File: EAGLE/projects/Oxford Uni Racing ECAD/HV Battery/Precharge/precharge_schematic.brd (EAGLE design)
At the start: 87.6 x 70.8 mm, 61 parts, among them IC1 TLV9001SIDCKR, IC10 74HC1G86GW-Q100H, IC11 74LVC1G32GV,125, IC2 TLV9001SIDCKR, IC3 TLV9001SIDCKR, IC4 TLV9001SIDCKR, IC5 LT1129CS8-3.3#PBF, IC6 LT1129CS8-3.3#PBF, IC7 LT1129CS8-3.3#PBF, IC8 LT1129CS8-3.3#PBF, IC9 74AHC1G08GV,125, J1 T816108A1S102CEU, Q1 BSS138, Q2 BSS138, U1 AMC1350QDWVRQ1AMC1350QDWVRQ1_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, U2 AMC1350QDWVRQ1AMC1350QDWVRQ1_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

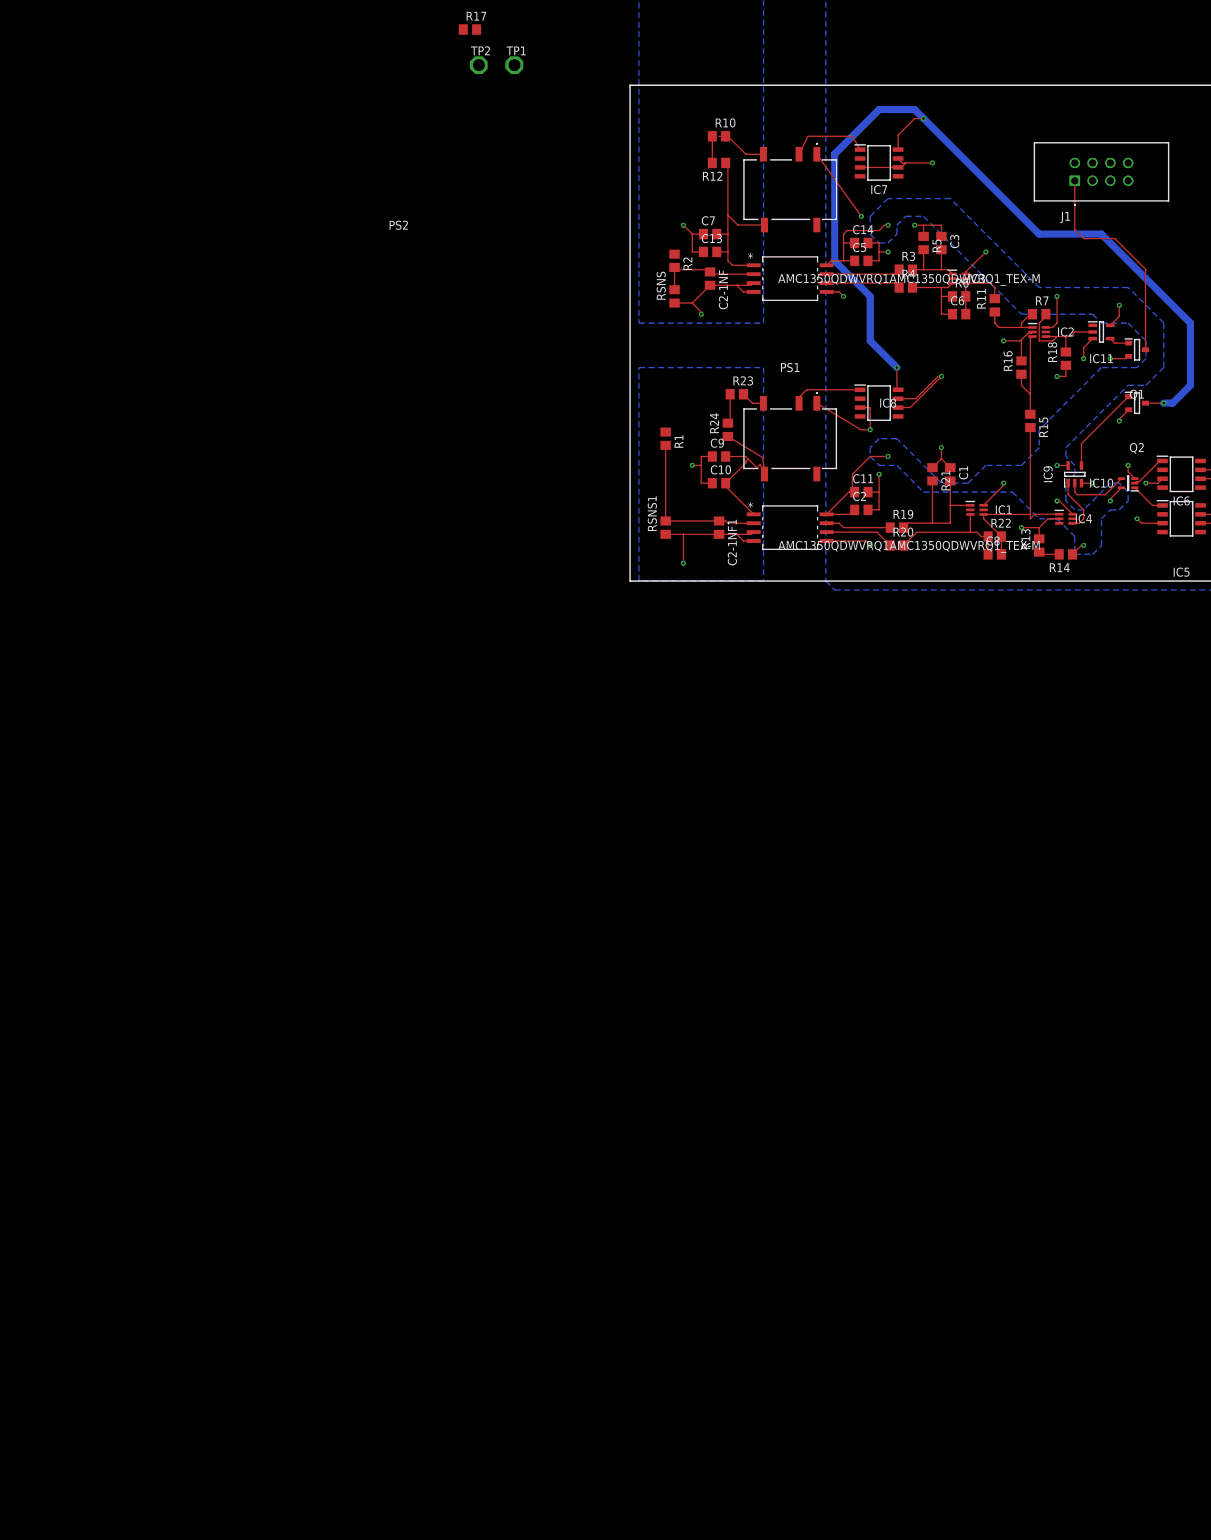
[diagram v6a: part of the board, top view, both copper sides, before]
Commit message: Library files + new main board/precharge board 8 pin mini-spox connector
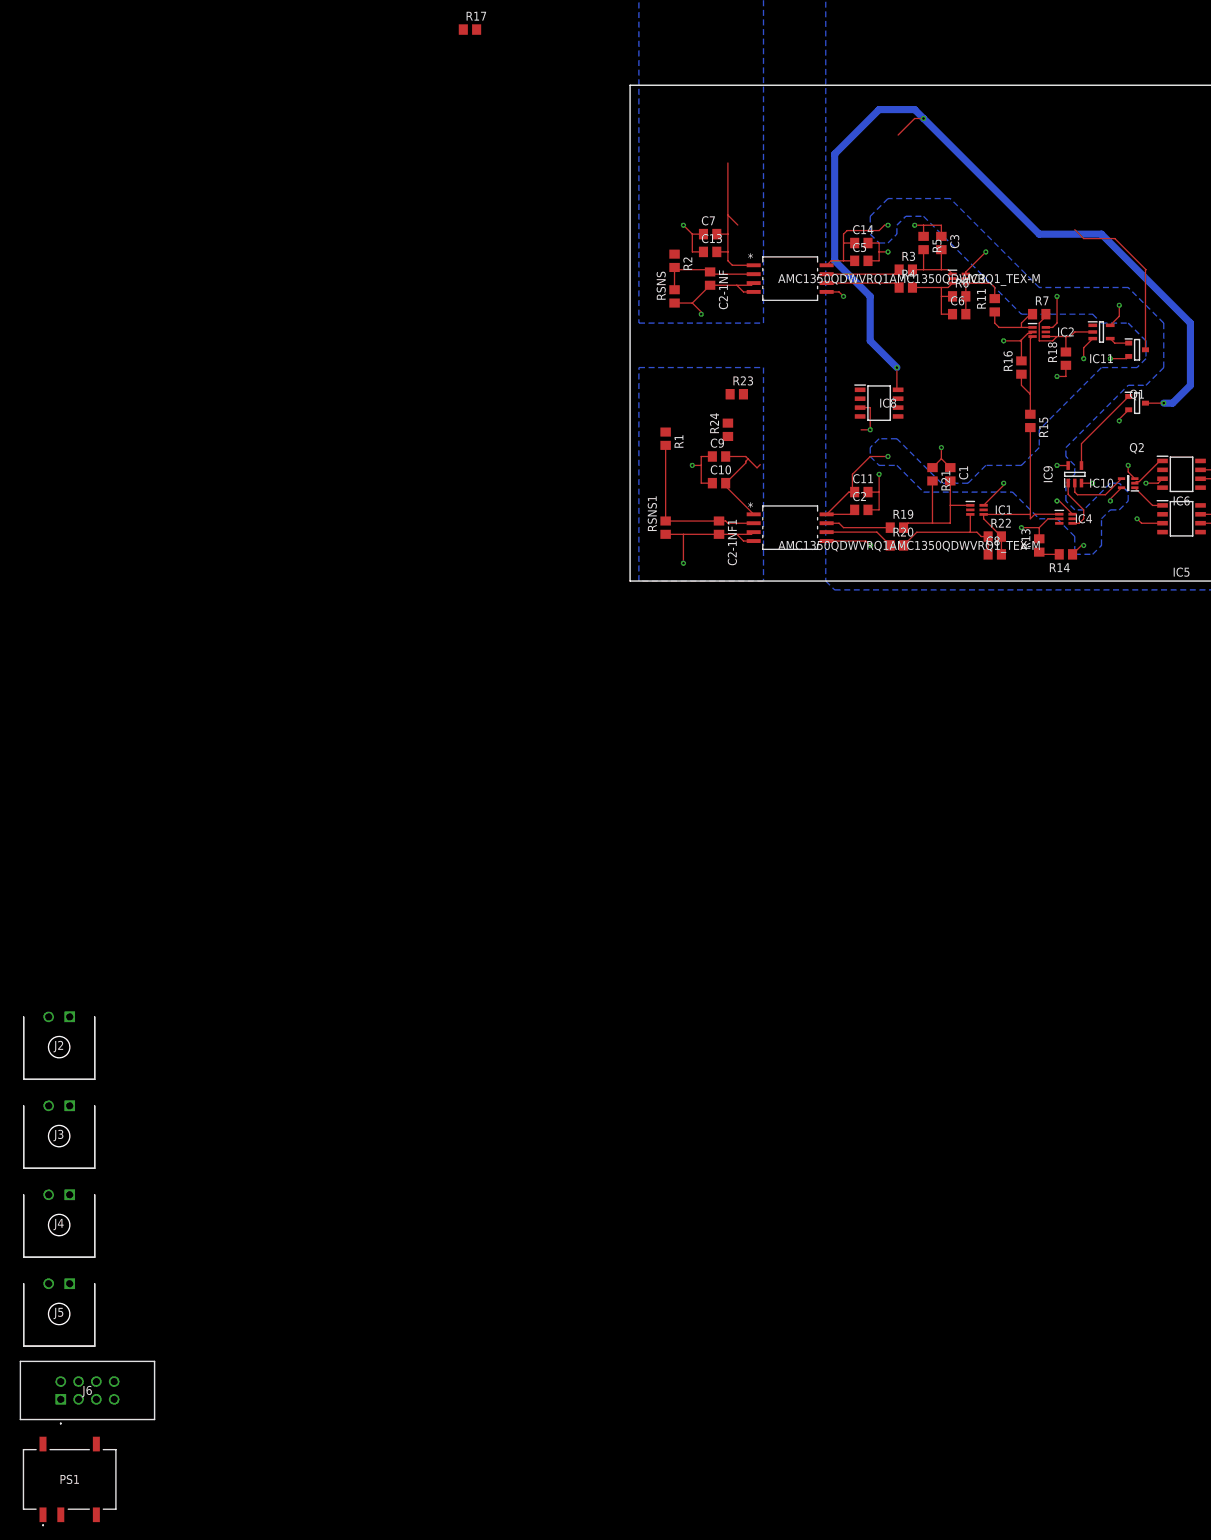
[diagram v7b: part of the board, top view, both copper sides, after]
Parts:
- removed IC7: LT1129CS8-3.3#PBF, LT1129CS8-3.3#PBF:SOIC127P599X175-8N
- removed J1: T816108A1S102CEU, T816108A1S102CEU:T816108A1S102CEU
- removed PS2: PDSE1-S12-S5-M-TR, PDSE1-S12-S5-M-TR:PDSE1S12S5MTR
- removed R10, R12: (no value), rcl:R0805
- removed TP1, TP2: PTR1PAD1-17, testpad:P1-17
- added J2, J3, J4, J5: 2-1445098-2, Micro-mate 2-1445098-2:214450982
- added J6: T816108A1S102CEU, T816108A1S102CEU:T816108A1S102CEU
- PS1: value PDSE1-S12-S5-M-TR -> PDSE1-S12-S12-M-TR; device PDSE1-S12-S5-M-TR:PDSE1S12S5MTR -> PDSE1-S12-S12-M-TR:PDSE1S12S12MTR
- moved PS1 180.7 mm to (-80.0, -128.3), turned to 0 degrees
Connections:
- removed net GND1: C13.1, C2-1NF.2, C7.1, RSNS.1, U1.3, U1.4
- removed net GND2: C10.1, C2-1NF1.2, C9.1, RSNS1.1, U2.3, U2.4
- removed net N$22: C13.2, C7.2, PS2.5, R12.1, U1.1
- removed net N$23: PS2.4, R10.2
- removed net N$24: IC7.1, PS2.2
- removed net N$25: R10.1, R12.2
- removed net N$30: IC8.1, PS1.2
- removed net N$40: J1.1, Q1.3
- new net GND(LV): C10.1, C13.1, C2-1NF.2, C2-1NF1.2, C7.1, C9.1, PS1.4, RSNS.1, RSNS1.1, U1.3, U1.4, U2.3, U2.4
- new net N$12: J2.1, J2.2
- new net N$14: J4.1, J4.2
- new net N$15: IC8.2, IC8.3
- new net N$20: IC8.8, PS1.5
- new net N$26: IC8.1, R23.2
- new net PRECHARGE_DECISION: J6.1, Q1.3
- new net TS+(CAR): J3.1, J3.2, R2.1
- new net TS+(CELLS): J5.1, J5.2, R1.1
- net +12V: now also PS1.2; no longer IC7.8, IC8.8
- net 3V3: now also IC1.5, IC2.5, IC3.5, IC4.5
- net GND: now also IC8.5; no longer IC7.3, IC7.6, IC7.7, IC8.3, PS2.1
- net N$28: no longer PS1.5
- net N$29: now also C13.2, C7.2, U1.1; no longer PS1.4, R23.2
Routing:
- net GND(LV): track 0.00 -> 52.8 mm, vias 0 -> 4
- net GND: track 125.0 -> 73.3 mm, vias 20 -> 16
- net N$40: track 31.0 -> 0.00 mm
- net GND2: track 27.9 -> 0.00 mm, vias 2 -> 0
- net N$22: track 27.2 -> 0.00 mm
- net GND1: track 24.9 -> 0.00 mm, vias 2 -> 0
- net PRECHARGE_DECISION: track 0.00 -> 24.0 mm
- net N$29: track 3.40 -> 23.1 mm
- net N$24: track 11.4 -> 0.00 mm
- net N$30: track 10.0 -> 0.00 mm
- net N$28: track 26.4 -> 16.7 mm
- net N$23: track 7.41 -> 0.00 mm
- net N$15: track 0.00 -> 5.92 mm, vias 0 -> 1
- net N$21: track 4.26 -> 0.00 mm
- net N$25: track 3.81 -> 0.00 mm
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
